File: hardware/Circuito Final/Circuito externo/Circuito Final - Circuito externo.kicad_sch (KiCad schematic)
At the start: 34 parts, among them J1 Conn_02x19_Odd_Even, J2 Conn_02x19_Odd_Even, J3 Conn_01x02, J4 Conn_01x02, SW1 SW_SPDT, SW2 SW_DIP_x04, U1 Opamp_Quad, U2 ICL7660

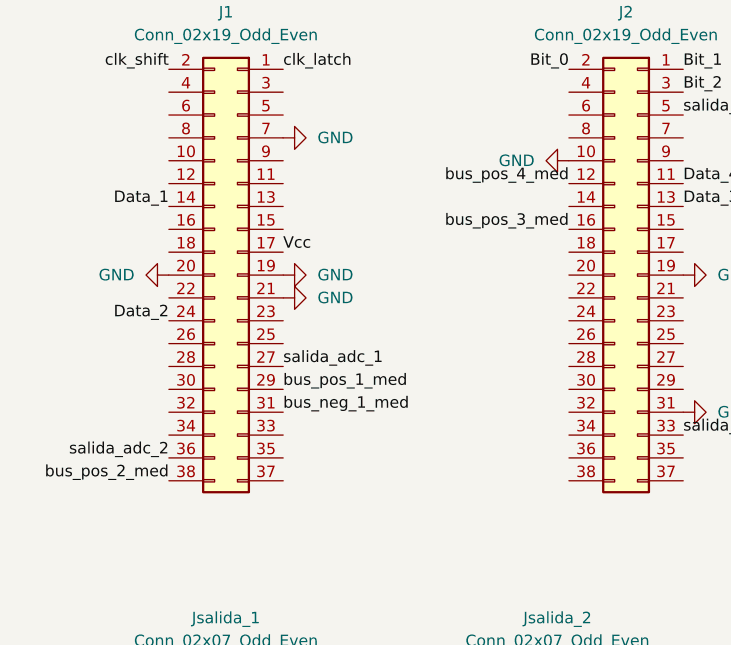
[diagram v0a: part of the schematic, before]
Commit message: update de esquemático y PCB del circuito externo
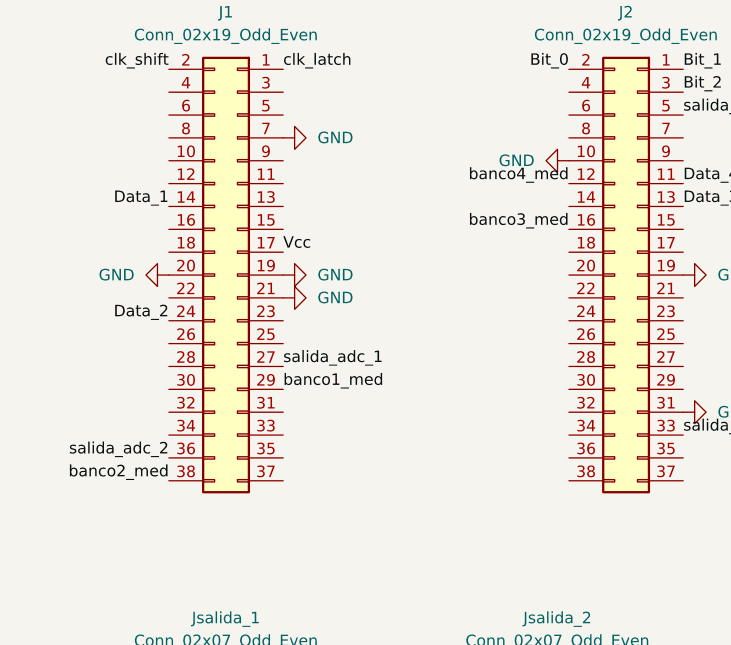
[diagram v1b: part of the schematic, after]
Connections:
- net bus_pos_1_med is gone; now on net banco1_med: J1.29 (Pin_29)
- net bus_pos_2_med is gone; now on net banco2_med: J1.38 (Pin_38)
- net bus_pos_3_med is gone; now on net banco3_med: J2.16 (Pin_16)
- net bus_pos_4_med is gone; now on net banco4_med: J2.12 (Pin_12)
- net bus_neg_1_med: no longer names the net of J1.31 (Pin_31)
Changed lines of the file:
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@@
+		)
+	)
+	(label "banco1_med"
+		(at 43.18 107.95 0)
+		(effects
+			(font
+				(size 1.27 1.27)
+			)
+			(justify left bottom)
 		)
 	)
@@
 		)
 	)
-	(label "bus_pos_1_med"
-		(at 43.18 107.95 0)
-		(effects
-			(font
-				(size 1.27 1.27)
-			)
-			(justify left bottom)
-		)
-	)
 	(label "bus_pos_3"
 		(at 161.29 113.03 180)
@@
 		)
 	)
+	(label "banco3_med"
+		(at 74.93 90.17 180)
+		(effects
+			(font
+				(size 1.27 1.27)
+			)
+			(justify right bottom)
+		)
+	)
 	(label "clk_shift"
 		(at 30.48 72.39 180)
@@
 		)
 	)
-	(label "bus_pos_4_med"
-		(at 74.93 85.09 180)
+	(label "banco2_med"
+		(at 30.48 118.11 180)
 		(effects
 			(font
@@
 		)
 	)
+	(label "banco4_med"
+		(at 74.93 85.09 180)
+		(effects
+			(font
+				(size 1.27 1.27)
+			)
+			(justify right bottom)
+		)
+	)
 	(label "bus_pos_3"
 		(at 104.14 144.78 180)
@@
 		)
 	)
-	(label "bus_pos_3_med"
-		(at 74.93 90.17 180)
-		(effects
-			(font
-				(size 1.27 1.27)
-			)
-			(justify right bottom)
-		)
-	)
 	(label "reset"
 		(at 153.67 152.4 0)
@@
 		)
 	)
-	(label "bus_pos_2_med"
-		(at 30.48 118.11 180)
-		(effects
-			(font
-				(size 1.27 1.27)
-			)
-			(justify right bottom)
-		)
-	)
 	(label "bus_pos_3"
 		(at 110.49 121.92 180)
@@
 		(effects
 			(font
-				(size 1.27 1.27)
-			)
-			(justify left bottom)
-		)
-	)
-	(label "bus_neg_1_med"
-		(at 43.18 110.49 0)
-		(effects
-			(font
